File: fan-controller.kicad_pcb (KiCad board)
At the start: 2 copper layers, 32 x 17 mm, 19 parts, among them J1 PWR, J2 PTC, J3 FAN, J4 Conn_ARM_SWD_TagConnect_TC203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, Q5 AO3400A, U1 L78L05, U2 PY32F002A

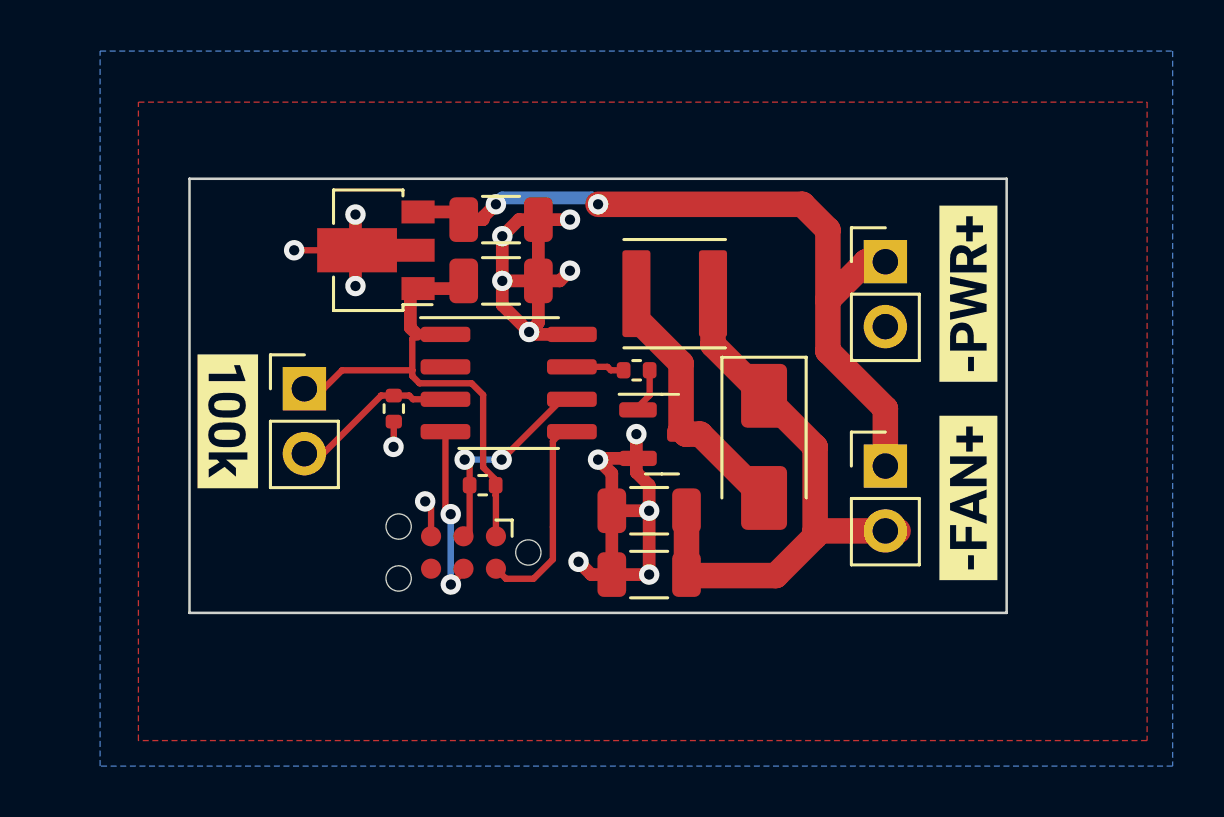
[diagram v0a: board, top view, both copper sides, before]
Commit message: Improve hardware reliability
Current sense + low-pass temperature filter at 100Hz cutoff
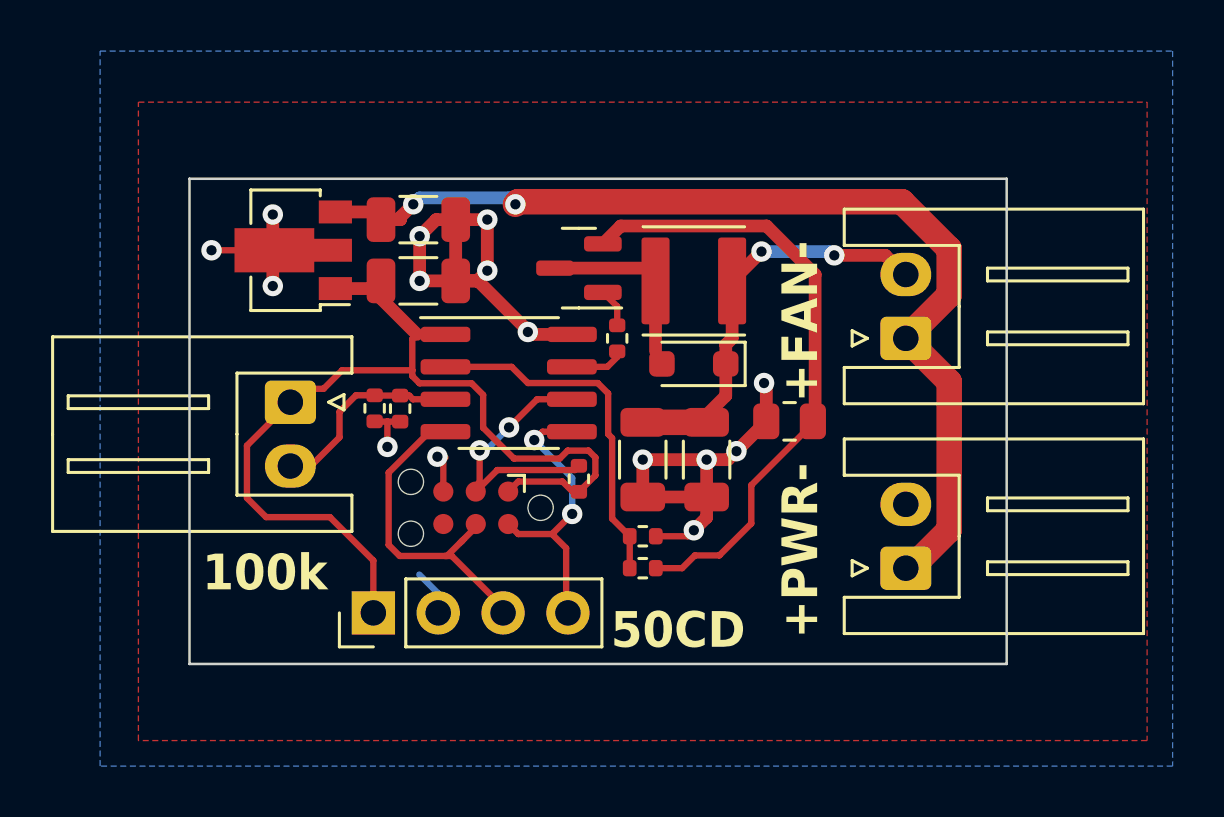
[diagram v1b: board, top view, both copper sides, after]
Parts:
- removed kibuzzard-1: G***, kibuzzard-63E173EF
- removed kibuzzard-2: G***, kibuzzard-63E17401
- removed kibuzzard-3: G***, kibuzzard-63E173E4
- added C5: 10n, Resistor_SMD:R_0402_1005Metric, F.Cu at (116.2, 66.0)
- added C6: 10n, Resistor_SMD:R_0402_1005Metric, F.Cu at (105.8, 61.0)
- added J5: Conn_01x04, Connector_PinHeader_2.54mm:PinHeader_1x04_P2.54mm_Vertical, F.Cu at (105.7, 69.0)
- added R2: 1, Resistor_SMD:R_0805_2012Metric, F.Cu at (122.0, 61.5)
- added R3: 100k, Resistor_SMD:R_0402_1005Metric, F.Cu at (116.2, 67.2)
- D1: value SS14 -> 1N5819WS; footprint Diode_SMD:D_SMA -> Diode_SMD:D_SOD-323_HandSoldering
- J1, J2, J3: footprint Connector_PinHeader_2.54mm:PinHeader_1x02_P2.54mm_Vertical -> Connector_JST:JST_XH_S2B-XH-A_1x02_P2.50mm_Horizontal
- moved J1 12.0 mm to (126.5, 67.2), turned to 90 degrees
- moved Q5 7.27 mm to (113.8, 55.5), turned to 180 degrees
- moved J3 5.06 mm to (126.5, 58.2), turned to 90 degrees
- moved C3 5.03 mm to (118.8, 63.0), turned to -90 degrees
- moved D1 4.26 mm to (118.2, 59.2), turned to 180 degrees
- moved R4 3.78 mm to (113.8, 63.8), turned to -90 degrees
- moved C1 3.24 mm to (107.5, 53.6)
- moved C2 3.24 mm to (107.5, 56.0)
- moved U1 3.24 mm to (102.3, 54.8)
- moved C4 2.02 mm to (116.2, 63.0), turned to -90 degrees
- moved J4 1.81 mm to (109.7, 64.9)
- moved R5 1.46 mm to (115.2, 58.2), turned to 90 degrees
- moved L1 0.90 mm to (118.2, 56.0)
- moved J2 0.76 mm to (102.5, 60.8), turned to -90 degrees
- moved R1 0.25 mm to (106.8, 61.0)
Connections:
- Q5 pad 2: GND -> Net-(Q5-S)
- U2 pad 2: unconnected-(U2-PA4/PA10-Pad2) -> /ISENSE
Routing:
- net Net-(Q5-S): track 0.00 -> 23.8 mm
- net +5V: track 20.1 -> 38.3 mm
- net /ISENSE: track 0.00 -> 14.0 mm
- net VPP: track 29.7 -> 39.5 mm
- net /FAN_OUT-: track 22.0 -> 16.4 mm, vias 0 -> 2
- net /SWCLK: track 6.89 -> 12.5 mm, vias 2 -> 0
- net /SWDIO: track 7.72 -> 11.2 mm, vias 0 -> 2
- net Net-(D1-A): track 9.39 -> 6.44 mm
- net /~{RST}: track 7.77 -> 10.3 mm
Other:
- board size 32 x 17 mm -> 32 x 19 mm
- board text added: "+FAN-"
- board text added: "+PWR-"
- board text added: "100k"
- board text added: "50CD"

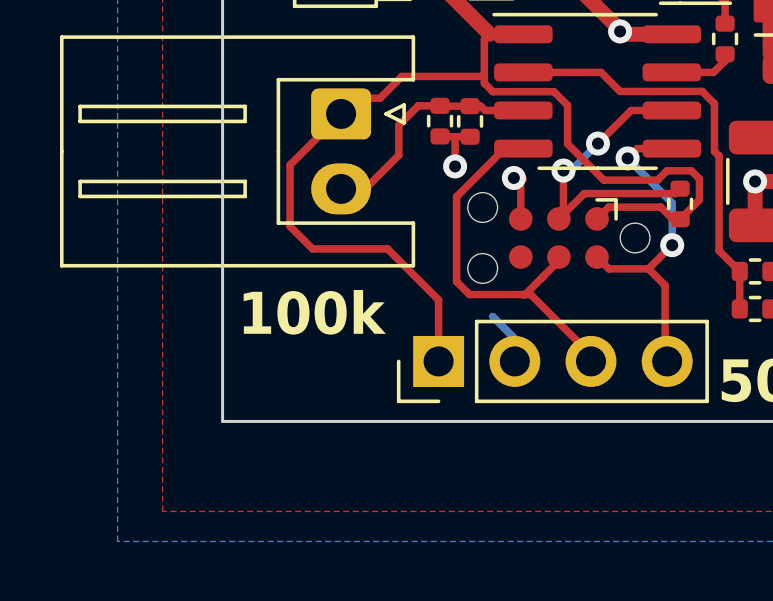
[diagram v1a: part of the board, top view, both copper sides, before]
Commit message: Switch to 10k thermistor in hardware
easier to find, and the on-board resistor is still 100kΩ so power
consumption is still low
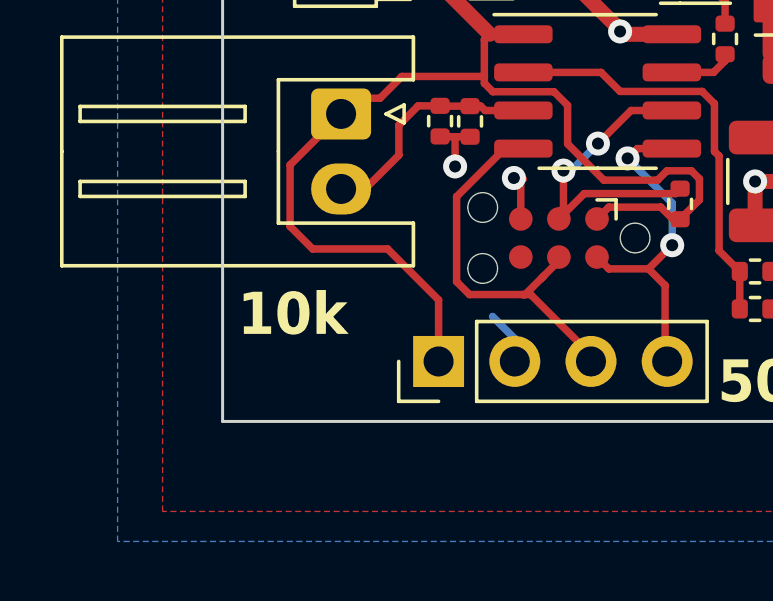
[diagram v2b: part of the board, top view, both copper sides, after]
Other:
- board text added: "10k"
- board text removed: "100k"
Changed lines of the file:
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@@
     (effects (font (size 1.4 1.3) (thickness 0.3) bold) (justify left bottom))
   )
-  (gr_text "100k" (at 99 68.25) (layer "F.SilkS" knockout)
+  (gr_text "10k" (at 99 68.25) (layer "F.SilkS" knockout)
     (effects (font (size 1.4 1.3) (thickness 0.3) bold) (justify left bottom))
   )
